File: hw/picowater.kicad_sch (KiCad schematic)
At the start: 48 parts, among them J1 +12V, J10 Batt TP, J11 Humidity, J12 Ultrasound, J2 Power In, J3 +5V Pins, J4 UART, J5 Power Out, J6 JST-PH2 Bat, J7 GPIO2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

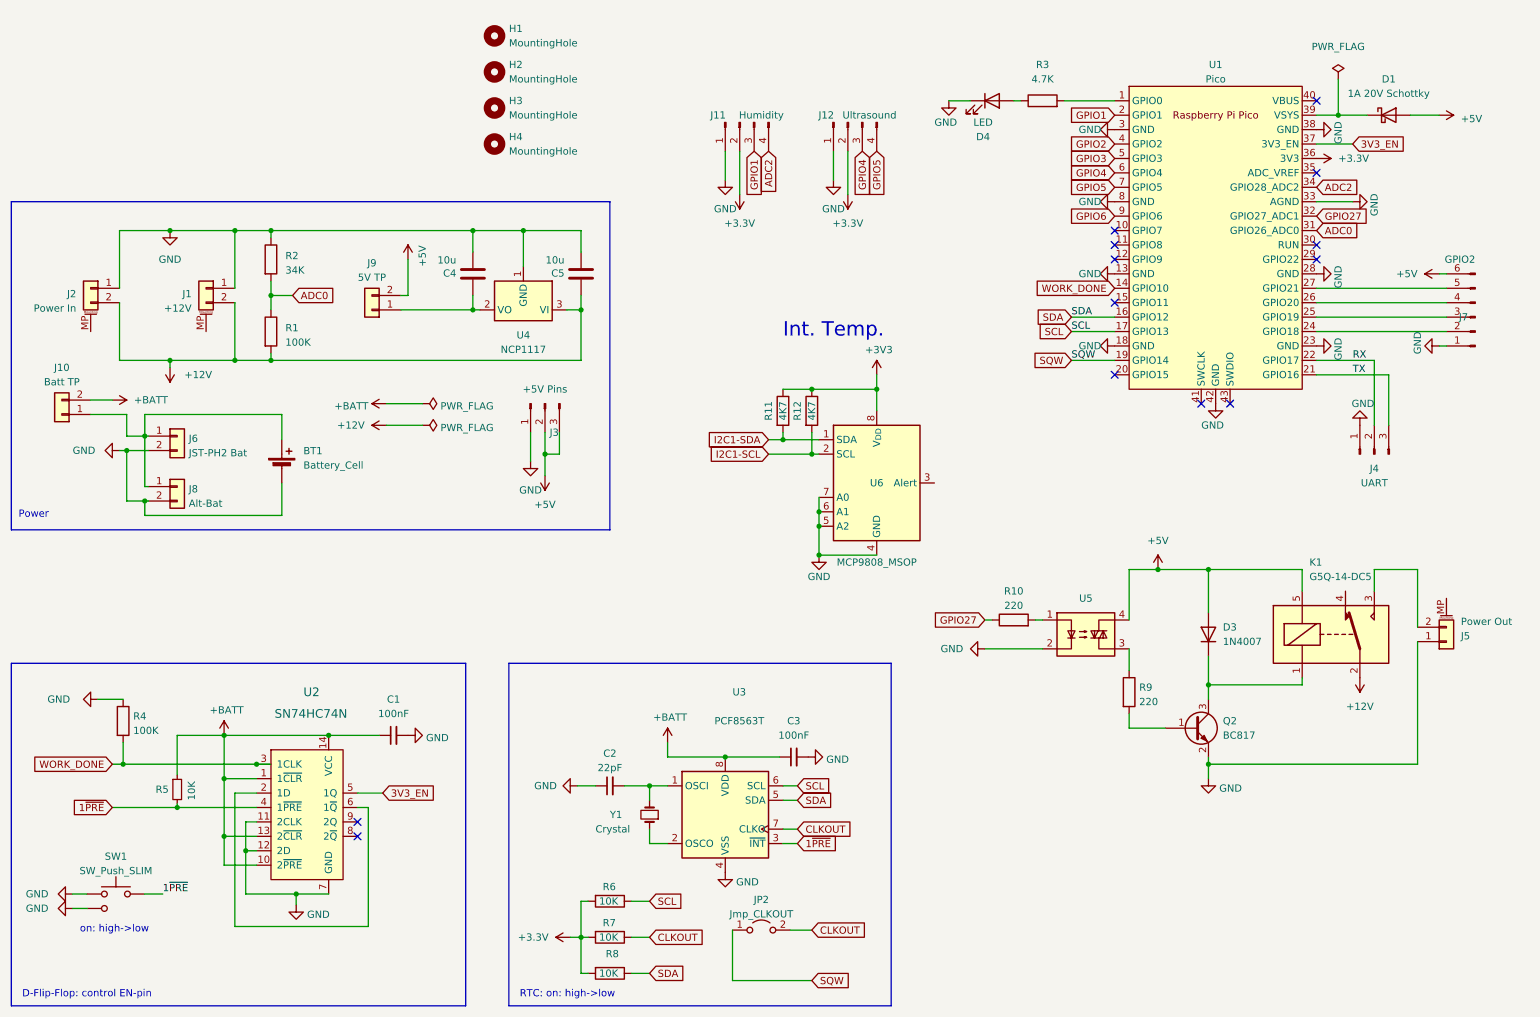
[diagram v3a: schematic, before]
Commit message: [pcb] add internal temp sensor
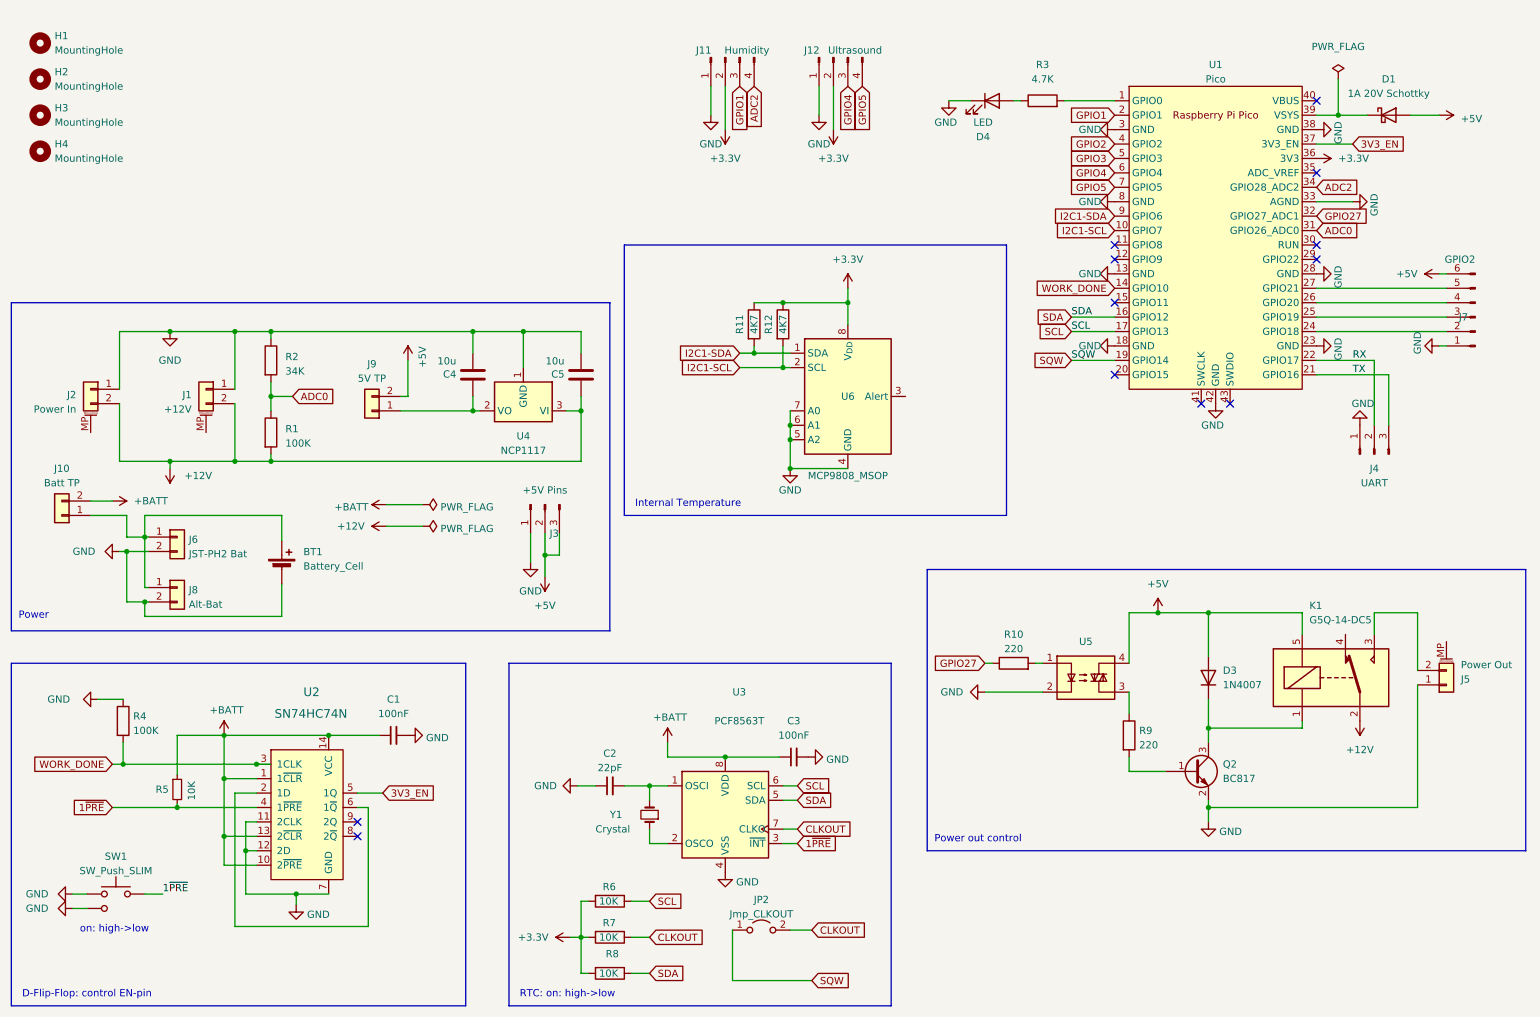
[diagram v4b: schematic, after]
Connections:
- net +3V3 is gone; now on net +3.3V: R11.1, R12.1, U6.8 (V_{DD})
- net GPIO6 is gone; now on net I2C1-SDA: U1.9 (GPIO6)
- net I2C1-SCL: now also U1.10 (GPIO7)
- no-connect marks 13 -> 12
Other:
- note added: "Internal Temperature"
- note added: "Power out control"
- note removed: "Int. Temp."
- moved on the sheet: BT1, C4, C5, D3, H1, H2, H3, H4, J1, J10, J11, J12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

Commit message: [pcb] lots of fixes and simplification
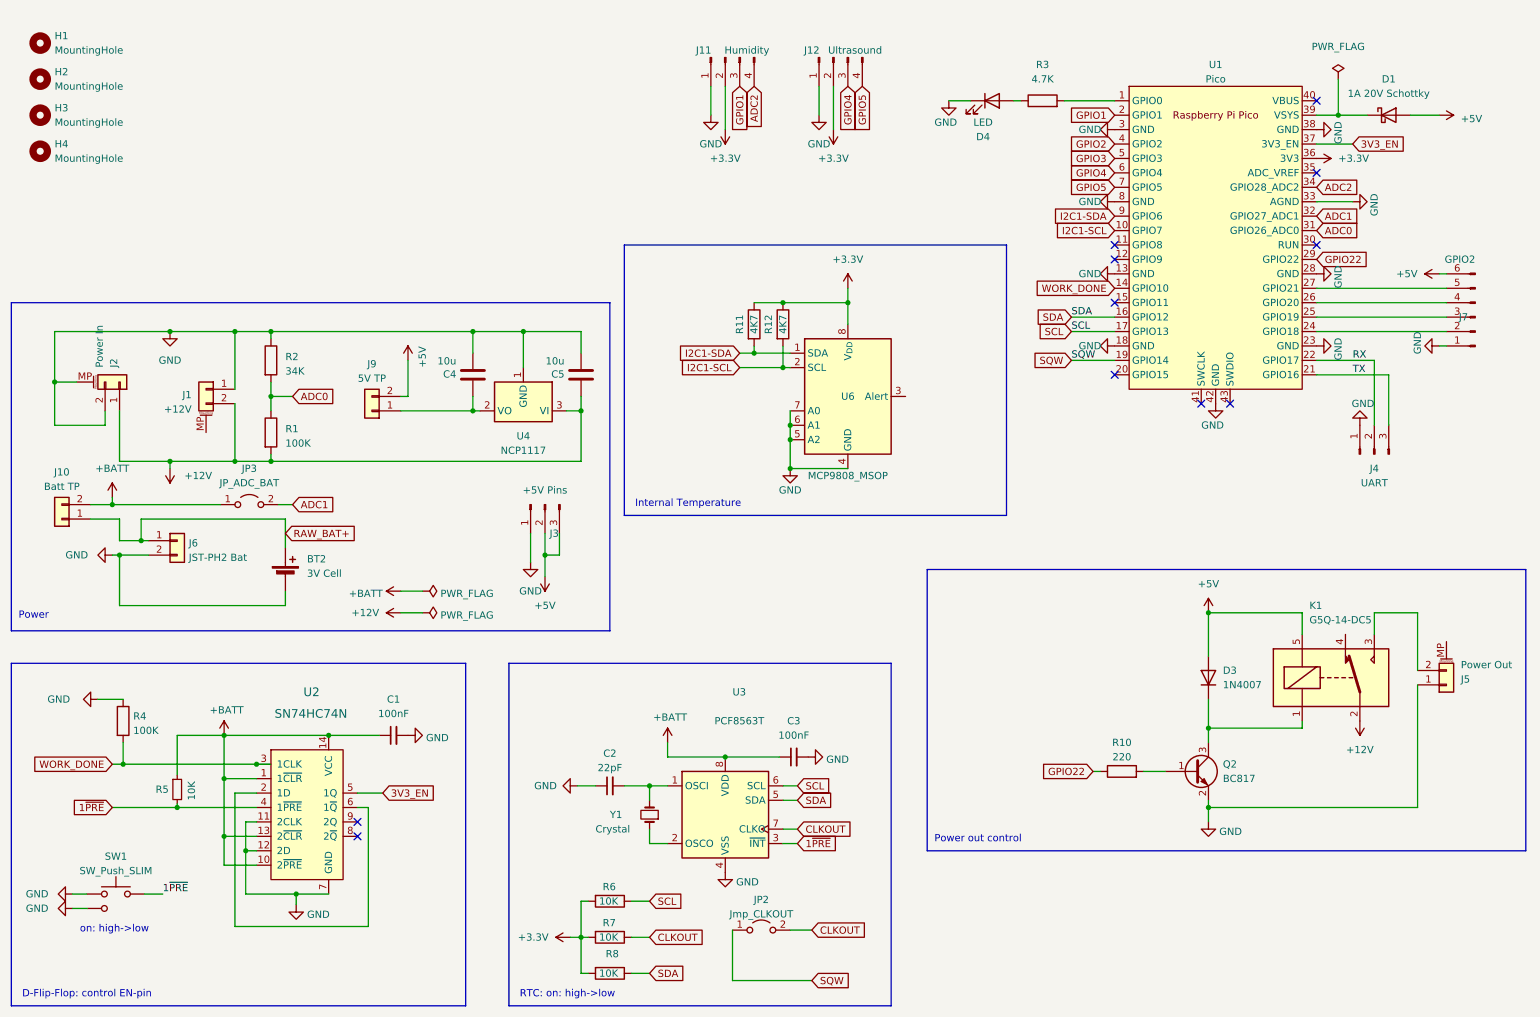
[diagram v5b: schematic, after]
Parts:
- removed BT1: Battery_Cell, Lunasys_Library:CR2032_Vertical_TE_1775485-1, symbol Device:Battery_Cell
- removed J8: Alt-Bat, Connector_PinHeader_2.54mm:PinHeader_1x02_P2.54mm_Vertical, symbol Connector_Generic:Conn_01x02
- removed R9: 220, Resistor_SMD:R_0402_1005Metric, symbol Device:R
- removed U5: ~, Package_DIP:SMDIP-4_W7.62mm, symbol Relay_SolidState:FODM3011
- added BT2: 3V Cell, cell:MPD_BC501SM-TR, symbol Device:Battery_Cell
- added JP3: JP_ADC_BAT, Jumper:SolderJumper-2_P1.3mm_Open_Pad1.0x1.5mm, symbol Jumper:Jumper_2_Open
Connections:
- net +12V: now also J2.1 (Pin_1); no longer J2.2 (Pin_2)
- net +BATT: now also JP3.1 (A)
- net GND: now also J2.2 (Pin_2), J2.MP (MountPin), BT2.2 (-); no longer J2.1 (Pin_1)
- net RAW_BAT+: now reaches J10.1 (Pin_1), J6.1 (Pin_1)
- net RAW_BAT+: now also BT2.1 (+)
- net GPIO22: now reaches U1.29 (GPIO22)
- net GPIO22: now also R10.1
- net at Q2.1 (B): now also R10.2
- net GPIO27 renamed ADC1
- net ADC1: now also JP3.2 (B); no longer R10.1
- no-connect marks 12 -> 11
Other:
- moved on the sheet: J10, J2, J6, R10

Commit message: [hw] new PCB with RJ45 as connector and other changes + case
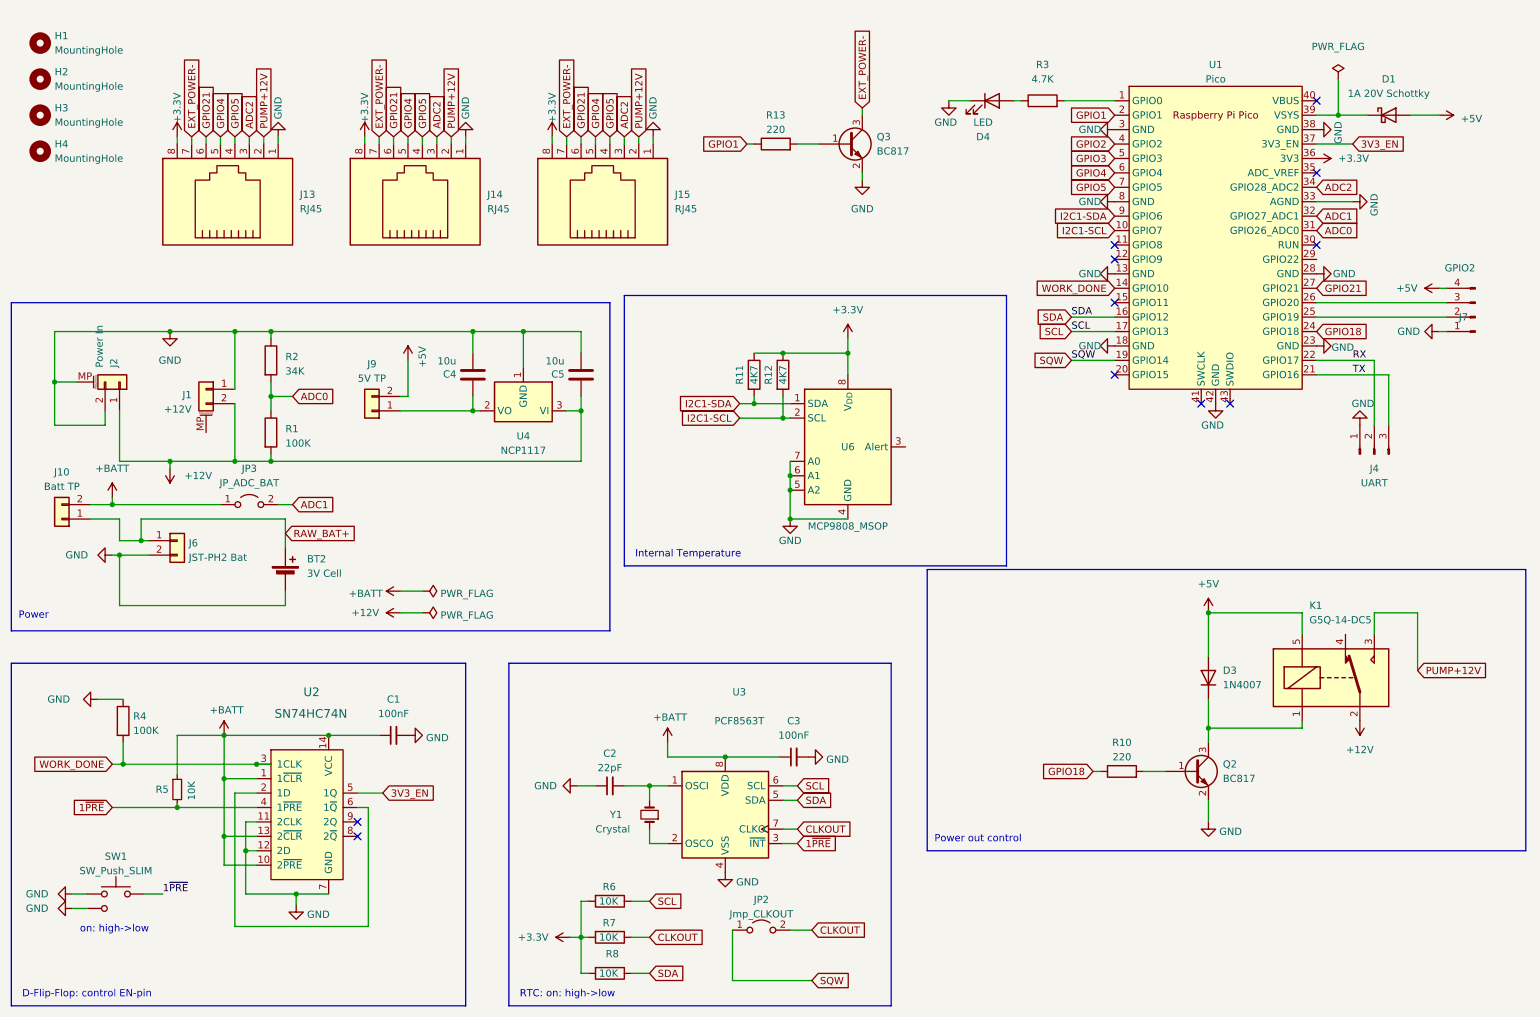
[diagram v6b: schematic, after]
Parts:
- removed J11: Humidity, Connector_PinHeader_2.54mm:PinHeader_1x04_P2.54mm_Horizontal, symbol Connector:Conn_01x04_Pin
- removed J12: Ultrasound, Connector_PinHeader_2.54mm:PinHeader_1x04_P2.54mm_Horizontal, symbol Connector:Conn_01x04_Pin
- removed J3: +5V Pins, Connector_PinHeader_2.54mm:PinHeader_1x03_P2.54mm_Vertical, symbol Connector:Conn_01x03_Pin
- removed J5: Power Out, Connector_PinHeader_2.54mm:PinHeader_1x02_P2.54mm_Vertical, symbol Connector_Generic_MountingPin:Conn_01x02_MountingPin
- added J13, J14, J15: RJ45, Connector_RJ:RJ45_BEL_SS74301-00x_Vertical, symbol Connector:RJ45
- added Q3: BC817, Package_TO_SOT_SMD:SOT-23, symbol Transistor_BJT:BC817
- added R13: 220, Resistor_SMD:R_0402_1005Metric, symbol Device:R
- BT2: footprint cell:MPD_BC501SM-TR -> cell:MPD_BC501SM-TR_custom
- H1, H2, H3, H4: footprint MountingHole:MountingHole_2.5mm -> MountingHole:MountingHole_4.3mm_M4
- J7: footprint Connector_PinHeader_2.54mm:PinHeader_1x06_P2.54mm_Vertical -> Connector_PinHeader_2.54mm:PinHeader_1x04_P2.54mm_Vertical; symbol Connector:Conn_01x06_Pin -> Connector:Conn_01x04_Pin
- SW1: footprint Button_Switch_THT:SW_PUSH_6mm -> Button_Switch_THT:SW_Tactile_SPST_Angled_PTS645Vx31-2LFS
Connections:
- net +3.3V: now also J13.8, J14.8, J15.8
- net +5V: now also J7.4 (Pin_4); no longer J7.6 (Pin_6)
- net ADC2: now also J13.3, J14.3, J15.3
- net GND: now also J13.1, J14.1, J15.1, Q3.2 (E)
- net GPIO1: now also R13.1
- net GPIO4: now also J13.5, J14.5, J15.5
- net GPIO5: now also J13.4, J14.4, J15.4
- net at J7.2 (Pin_2): now also U1.25 (GPIO19); no longer U1.24 (GPIO18)
- net at J7.3 (Pin_3): now also U1.26 (GPIO20); no longer U1.25 (GPIO19)
- net GPIO21: now reaches U1.27 (GPIO21)
- net GPIO21: now also J13.6, J14.6, J15.6; no longer J7.5 (Pin_5)
- net PUMP+12V: now reaches K1.3
- net PUMP+12V: now also J13.2, J14.2, J15.2
- net GPIO22: no longer names the net of U1.29 (GPIO22)
- net GPIO22: no longer R10.1
- new net: Q3.1 (B), R13.2
- new net EXT_POWER-: J13.7, J14.7, J15.7, Q3.3 (C)
- new net GPIO18: R10.1, U1.24 (GPIO18)
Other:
- moved on the sheet: R11, R12, U6

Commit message: fw: send info to server, pcb: many tweaks
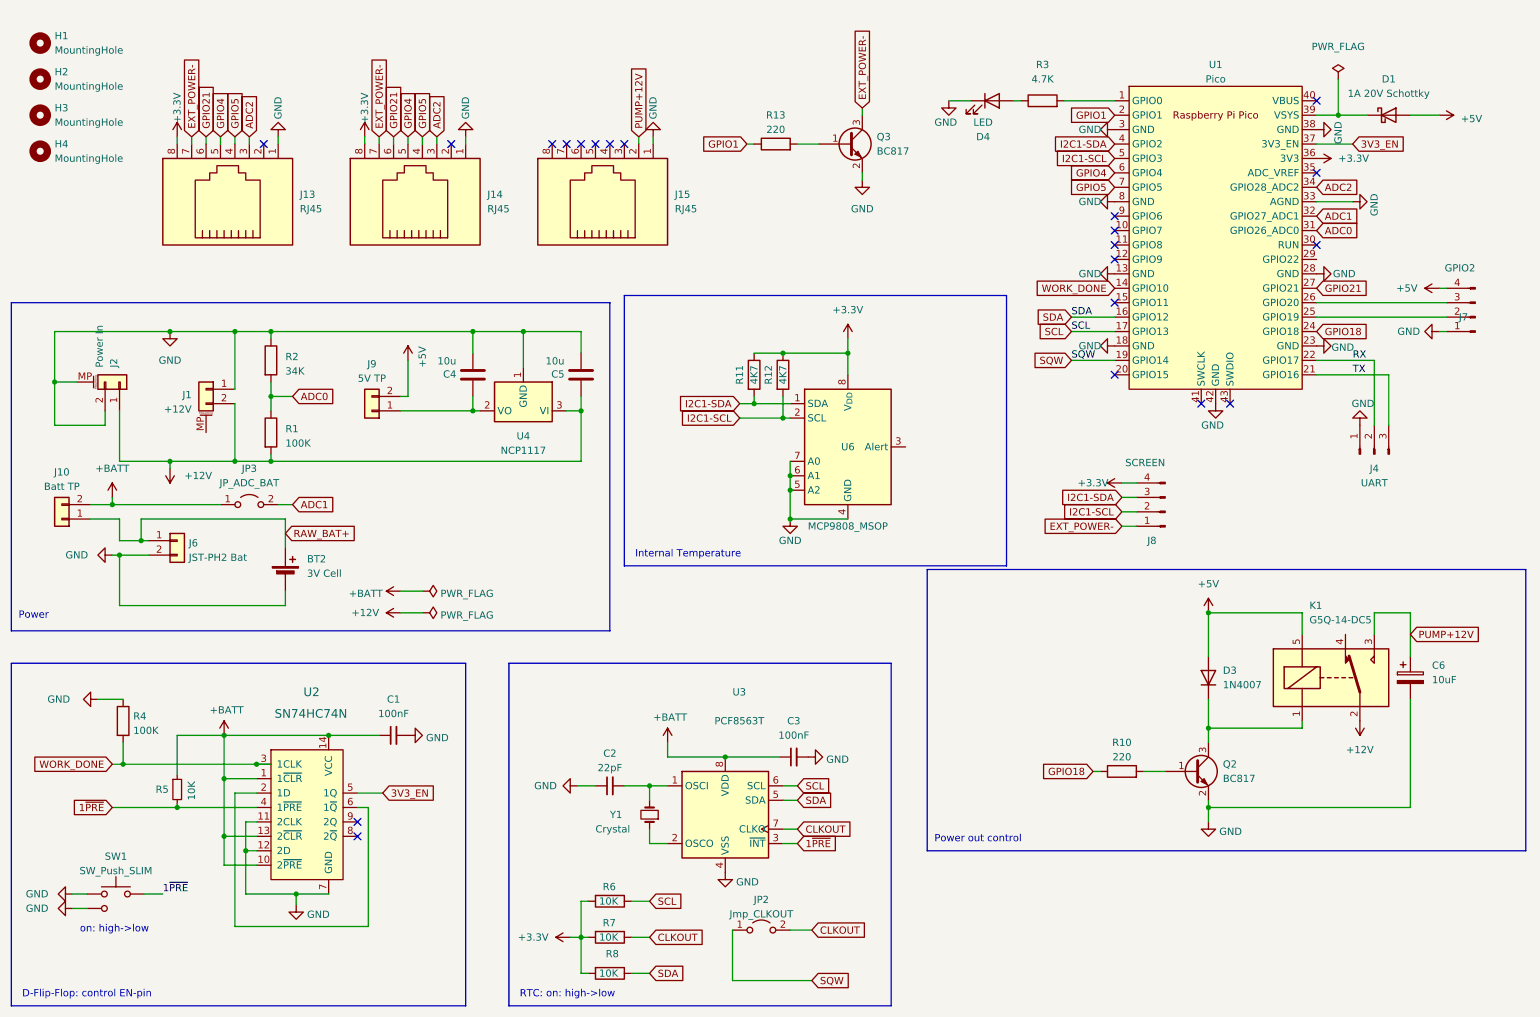
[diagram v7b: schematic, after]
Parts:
- added C6: 10uF, Capacitor_THT:CP_Radial_D8.0mm_P3.80mm, symbol Device:C_Polarized
- added J8: SCREEN, Connector_PinHeader_2.54mm:PinHeader_1x04_P2.54mm_Vertical, symbol Connector:Conn_01x04_Pin
- R11, R12: footprint Capacitor_SMD:C_0402_1005Metric -> Capacitor_SMD:C_0603_1608Metric
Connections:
- net GPIO2 is gone; now on net I2C1-SDA: U1.4 (GPIO2)
- net GPIO3 is gone; now on net I2C1-SCL: U1.5 (GPIO3)
- net +3.3V: now also J8.4 (Pin_4); no longer J15.8
- net ADC2: no longer J15.3
- net EXT_POWER-: now also J8.1 (Pin_1); no longer J15.7
- net GND: now also C6.2
- net GPIO21: no longer J15.6
- net GPIO4: no longer J15.5
- net GPIO5: no longer J15.4
- net I2C1-SCL: now also J8.2 (Pin_2); no longer U1.10 (GPIO7)
- net I2C1-SDA: now also J8.3 (Pin_3); no longer U1.9 (GPIO6)
- net PUMP+12V: now also C6.1; no longer J13.2, J14.2
- no-connect marks 11 -> 21

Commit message: [pcb] update
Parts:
- removed U4: NCP1117, Package_TO_SOT_SMD:SOT-223-3_TabPin2, symbol Regulator_Linear:NCP1117-5.0_SOT223
- added C7: 1u, Capacitor_SMD:C_0603_1608Metric, symbol Device:C
- added C8, C9: 0.1u, Capacitor_SMD:C_0603_1608Metric, symbol Device:C
- added D2: 11DQ06, symbol Device:D_Schottky
- added J3: 12V TP, Connector_PinHeader_2.54mm:PinHeader_1x02_P2.54mm_Vertical, symbol Connector_Generic:Conn_01x02
- added L1: 10uH, Capacitor_SMD:C_0805_2012Metric, symbol Device:L
- added L2: 330uH, symbol Device:L
- added U5: MAX77596, Lunasys_Library:TDFN-10-EP_2.5mm, symbol Lunasys_Library:MAX77596
- added U7: LM2574M-5, symbol Regulator_Switching:LM2574M-5
- C4: value 10u -> 22u
- H1, H2, H3, H4: footprint MountingHole:MountingHole_4.3mm_M4 -> Lunasys_Library:hole_5mm
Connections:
- net +12V: now also J3.1 (Pin_1); no longer C5.1, R1.2
- net +5V: now also J13.2, J14.2
- net 3V3_EN: now also U5.10 (EN)
- net GND: now also C7.1, C9.2, D2.2 (A), U5.11 (PAD), U5.4 (PGND), U5.5 (AGND), U7.4 (SGND), U7.6 (PGND)
- net N_3V3_EN: now reaches U2.2 (1D), U2.6 (1~{Q})
- net N_3V3_EN: now also U7.5 (~{ON}/OFF)
- net at C4.1, J9.1 (Pin_1): now also L1.2, L2.2, U5.9 (OUT/FB), U7.3 (FB)
- new net: D2.1 (K), L2.1, U7.12 (OUT)
- new net: C5.1, C9.1, J3.2 (Pin_2), R1.2, U5.2 (SUP), U7.10 (VIN)
- new net: C8.1, L1.1, U5.3 (LX)
- new net: C7.2, U5.8 (BIAS)
- new net: C8.2, U5.1 (BST)
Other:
- moved on the sheet: C4, C5, J1, J9, R11, R12, U6
